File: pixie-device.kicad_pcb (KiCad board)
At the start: 4 copper layers, 70 x 70 mm, 75 parts, among them U1 USBLC6-2SC6, U2 SPX3819M5-L-3-3, U3 W25Q128JVS, U4 ESP32-C3, U5 SN74LVC1T45DBV, Y1 40Mhz

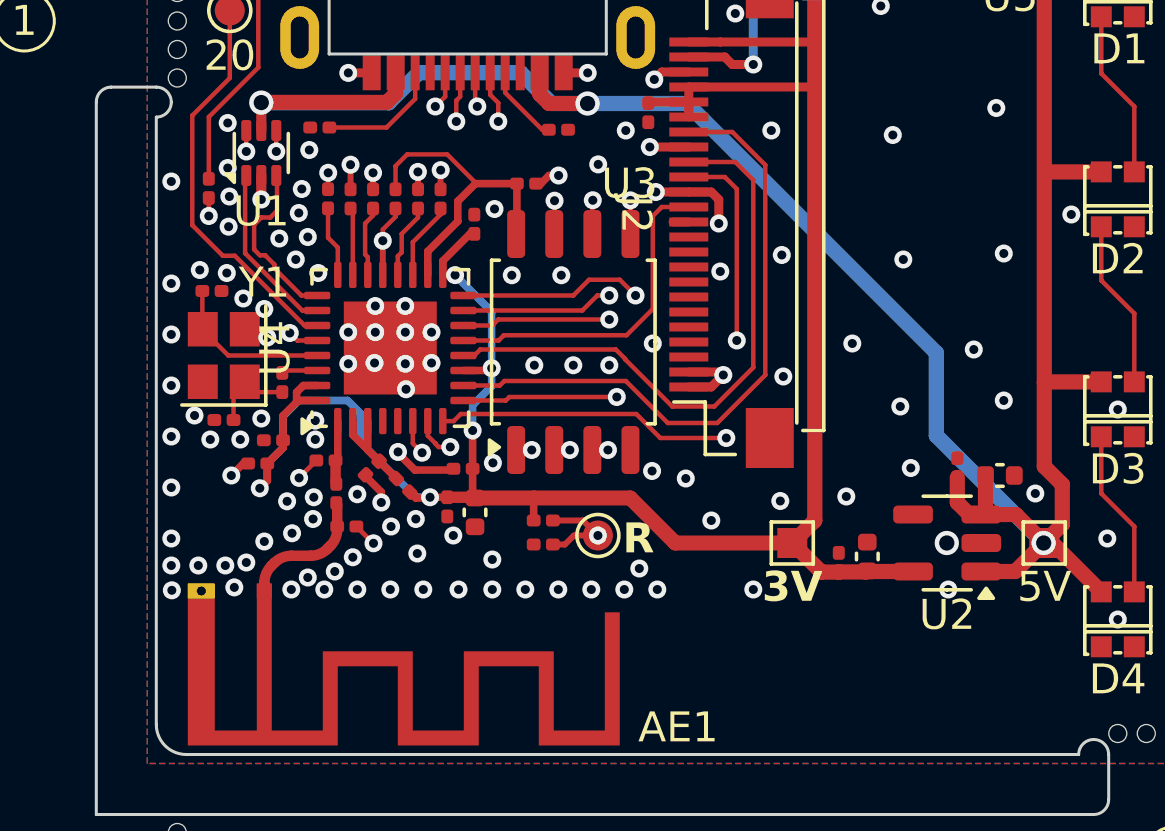
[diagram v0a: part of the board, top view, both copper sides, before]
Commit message: Use ESP suggested C3 footprint and update for KiCad 8.
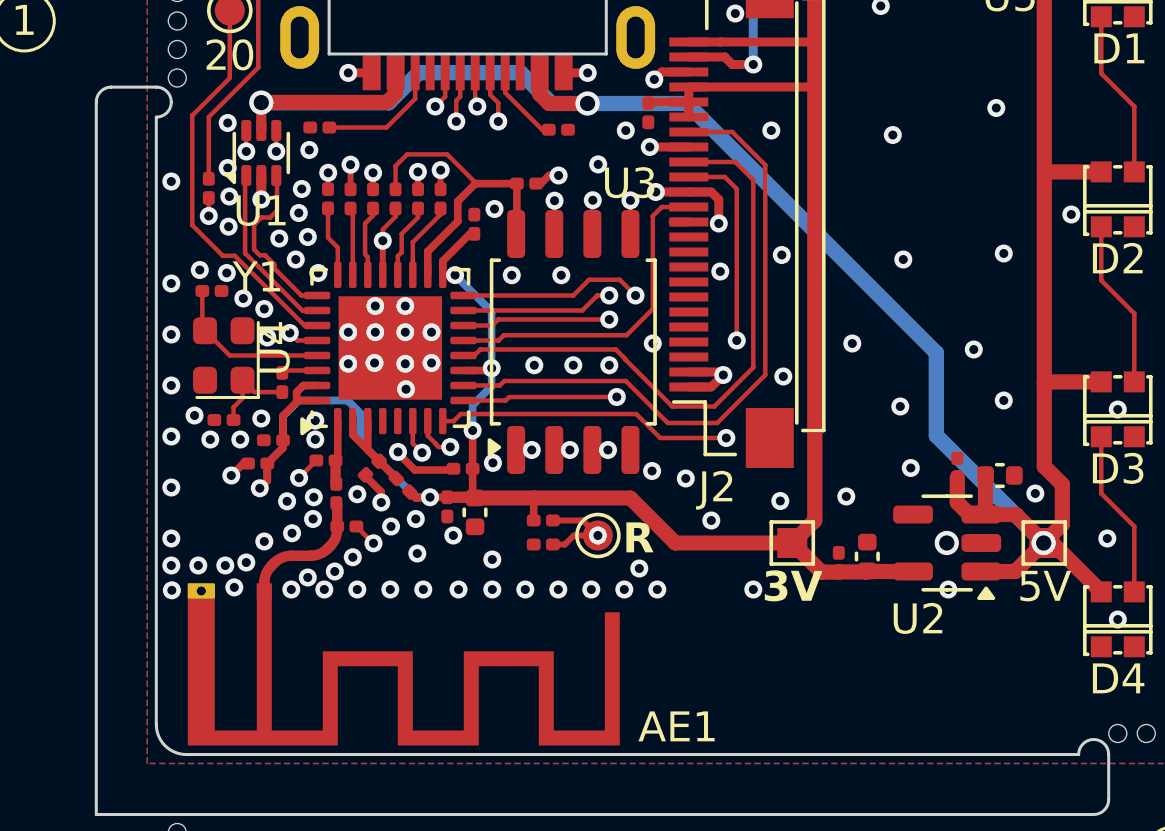
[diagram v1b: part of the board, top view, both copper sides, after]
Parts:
- removed branding-logo-1: logo-15mm, firefly:logo-15mm
- removed branding-name-1: text-10, firefly:text-10
- added REF**: text-10, firefly:text-10, B.Cu at (133.4, 85.0)
- added REF**: logo-15mm, firefly:logo-15mm, B.Cu at (133.1, 78.0)
- U4: footprint Package_DFN_QFN:QFN-32-1EP_5x5mm_P0.5mm_EP3.1x3.1mm -> Package_DFN_QFN:QFN-32-1EP_5x5mm_P0.5mm_EP3.45x3.45mm
- Y1: footprint Crystal:Crystal_SMD_2520-4Pin_2.5x2.0mm -> firefly:crystal_2520

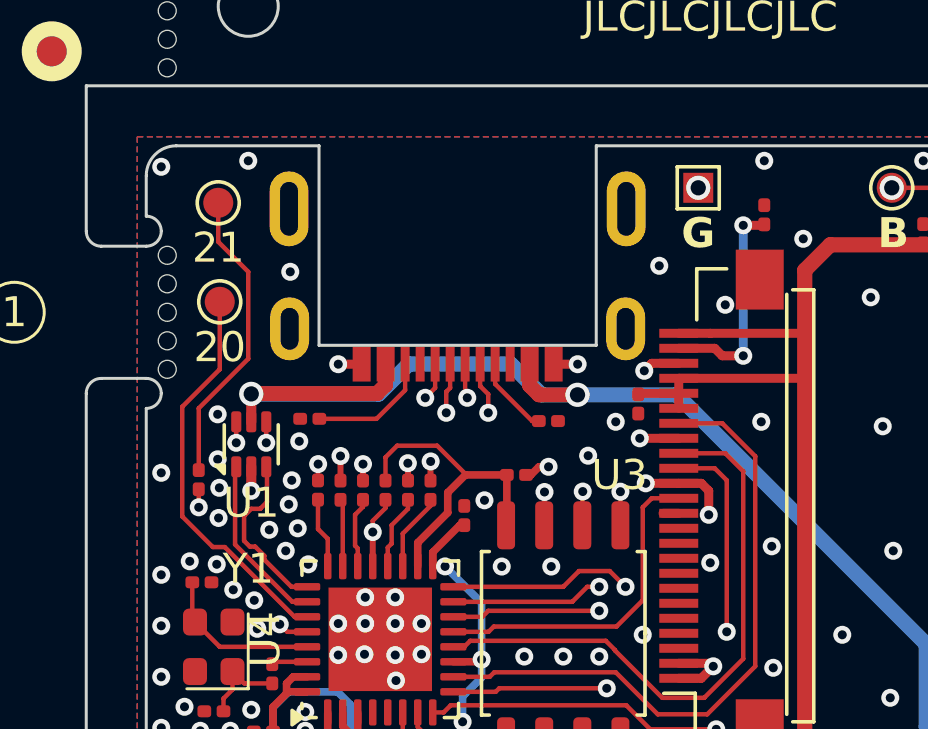
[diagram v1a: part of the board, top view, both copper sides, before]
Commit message: Moved GPIO 20 and 21 around.
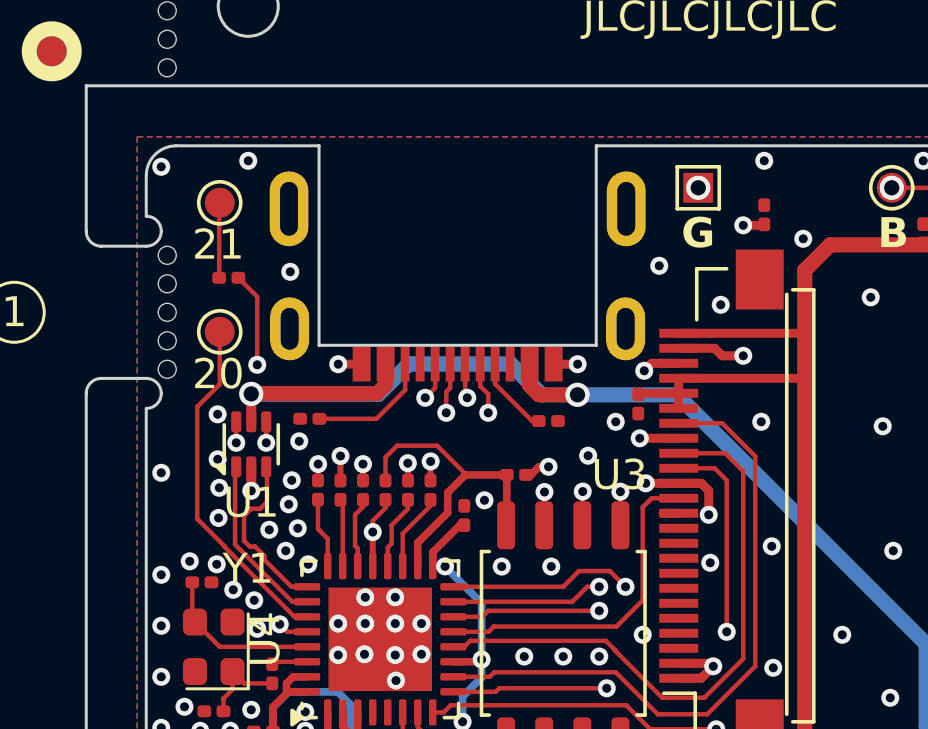
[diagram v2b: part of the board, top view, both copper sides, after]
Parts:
- moved R11 6.80 mm to (102.8, 74.4), turned to 180 degrees
- moved TP1 1.00 mm to (102.5, 76.2)
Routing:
- net Net-(U4-U0TXD/GPIO21): track 6.63 -> 15.1 mm
- net /MCU/IO21: track 10.0 -> 2.51 mm
- net /MCU/IO20: track 13.2 -> 11.6 mm
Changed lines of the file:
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@@
 	(footprint "TestPoint:TestPoint_Pad_D1.0mm"
 		(layer "F.Cu")
-		(at 102.4 71.9)
+		(at 102.45 71.9)
 		(descr "SMD pad as test Point, diameter 1.0mm")
 		(tags "test point SMD pad")
@@
 			(thermal_bridge_angle 45)
 		)
+		(model "${KIPRJMOD}/kicad-components/3d-models/usb-c-sink-8.wrl"
+			(offset
+				(xyz 0 0 0)
+			)
+			(scale
+				(xyz 1 1 1)
+			)
+			(rotate
+				(xyz 0 0 0)
+			)
+		)
 	)
 	(footprint "Capacitor_SMD:C_0201_0603Metric"
@@
 	(footprint "TestPoint:TestPoint_Pad_D1.0mm"
 		(layer "F.Cu")
-		(at 102.45 75.2)
+		(at 102.45 76.2)
 		(descr "SMD pad as test Point, diameter 1.0mm")
 		(tags "test point SMD pad")
@@
 	(footprint "Resistor_SMD:R_0201_0603Metric"
 		(layer "F.Cu")
-		(at 101.75 81.13 90)
+		(at 102.75 74.4 180)
 		(descr "Resistor SMD 0201 (0603 Metric), square (rectangular) end terminal, IPC_7351 nominal, (Body size source: https://www.vishay.com/docs/20052/crcw0201e3.pdf), generated with kicad-footprint-generator")
 		(tags "resistor")
 		(property "Reference" "R11"
-			(at 0 -1.05 90)
+			(at 0 -1.05 180)
 			(layer "F.SilkS")
 			(hide yes)
@@
 		)
 		(property "Value" "499R"
-			(at 0 1.05 90)
+			(at 0 1.05 180)
 			(layer "F.Fab")
 			(effects
@@
 		)
 		(property "Footprint" "Resistor_SMD:R_0201_0603Metric"
-			(at 0 0 90)
+			(at 0 0 180)
 			(unlocked yes)
 			(layer "F.Fab")
@@
 		)
 		(property "Datasheet" ""
-			(at 0 0 90)
+			(at 0 0 180)
 			(unlocked yes)
 			(layer "F.Fab")
@@
 		)
 		(property "Description" ""
-			(at 0 0 90)
+			(at 0 0 180)
 			(unlocked yes)
 			(layer "F.Fab")
@@
 		)
 		(property "MPN" "C4354889"
-			(at 0 0 0)
+			(at 0 0 270)
 			(layer "F.Fab")
 			(hide yes)
@@
 		(attr smd)
 		(fp_line
-			(start 0.7 -0.35)
-			(end 0.7 0.35)
+			(start 0.7 0.35)
+			(end -0.7 0.35)
 			(stroke
 				(width 0.05)
@@
 		)
 		(fp_line
-			(start -0.7 -0.35)
-			(end 0.7 -0.35)
+			(start 0.7 -0.35)
+			(end 0.7 0.35)
 			(stroke
 				(width 0.05)
@@
 		)
 		(fp_line
-			(start 0.7 0.35)
-			(end -0.7 0.35)
+			(start -0.7 0.35)
+			(end -0.7 -0.35)
 			(stroke
 				(width 0.05)
@@
 		)
 		(fp_line
-			(start -0.7 0.35)
-			(end -0.7 -0.35)
+			(start -0.7 -0.35)
+			(end 0.7 -0.35)
 			(stroke
 				(width 0.05)
@@
 		)
 		(fp_line
-			(start 0.3 -0.15)
-			(end 0.3 0.15)
+			(start 0.3 0.15)
+			(end -0.3 0.15)
 			(stroke
 				(width 0.1)
@@
 		)
 		(fp_line
-			(start -0.3 -0.15)
-			(end 0.3 -0.15)
+			(start 0.3 -0.15)
+			(end 0.3 0.15)
 			(stroke
 				(width 0.1)
@@
 		)
 		(fp_line
-			(start 0.3 0.15)
-			(end -0.3 0.15)
+			(start -0.3 0.15)
+			(end -0.3 -0.15)
 			(stroke
 				(width 0.1)
@@
 		)
 		(fp_line
-			(start -0.3 0.15)
-			(end -0.3 -0.15)
+			(start -0.3 -0.15)
+			(end 0.3 -0.15)
 			(stroke
 				(width 0.1)
@@
 		)
 		(fp_text user "${REFERENCE}"
-			(at 0 -0.68 90)
+			(at 0 -0.68 180)
 			(layer "F.Fab")
 			(effects
@@
 		)
 		(pad "" smd roundrect
-			(at -0.345 0 90)
+			(at -0.345 0 180)
 			(size 0.318 0.36)
 			(layers "F.Paste")
@@
 		)
 		(pad "" smd roundrect
-			(at 0.345 0 90)
+			(at 0.345 0 180)
 			(size 0.318 0.36)
 			(layers "F.Paste")
@@
 		)
 		(pad "1" smd roundrect
-			(at -0.32 0 90)
+			(at -0.32 0 180)
 			(size 0.46 0.4)
 			(layers "F.Cu" "F.Mask")
@@
 		)
 		(pad "2" smd roundrect
-			(at 0.32 0 90)
+			(at 0.32 0 180)
 			(size 0.46 0.4)
 			(layers "F.Cu" "F.Mask")
@@
 	)
 	(gr_text "20"
-		(at 102.45 77.3 0)
+		(at 102.4 78.2 0)
 		(layer "F.SilkS")
 		(effects
@@
 	)
 	(gr_text "21"
-		(at 102.4 73.4 0)
+		(at 102.4 73.3 0)
 		(layer "F.SilkS")
 		(effects
@@
 	)
 	(via
-		(at 119.3 75.3)
+		(at 119.15 75.3)
 		(size 0.6)
 		(drill 0.3)
@@
 	)
 	(segment
-		(start 103.4 74.2)
-		(end 102.4 73.2)
-		(width 0.15)
-		(layer "F.Cu")
-		(net 38)
-	)
-	(segment
-		(start 102.4 73.2)
-		(end 102.4 71.9)
+		(start 102.45 71.9)
+		(end 102.43 71.92)
 		(width 0.15)
 		(layer "F.Cu")
@@
 	)
 	(segment
-		(start 103.4 77.1)
-		(end 103.4 74.2)
-		(width 0.15)
-		(layer "F.Cu")
-		(net 38)
-	)
-	(segment
-		(start 101.75 78.75)
-		(end 103.4 77.1)
-		(width 0.15)
-		(layer "F.Cu")
-		(net 38)
-	)
-	(segment
-		(start 101.75 80.81)
-		(end 101.75 78.75)
+		(start 102.43 71.92)
+		(end 102.43 74.4)
 		(width 0.15)
 		(layer "F.Cu")
@@
 		(end 119.9 72.65)
 		(width 0.3)
-		(layer "B.Cu")
+		(layer "In2.Cu")
 		(net 50)
 	)
@@
 	)
 	(segment
-		(start 101.75 82.05)
-		(end 101.75 81.45)
+		(start 103.7 77.3)
+		(end 103.7 75.03)
+		(width 0.15)
+		(layer "F.Cu")
+		(net 51)
+	)
+	(segment
+		(start 103.7 75.03)
+		(end 103.07 74.4)
 		(width 0.15)
 		(layer "F.Cu")
@@
 	)
 	(via
-		(at 101.75 82.05)
+		(at 103.7 77.3)
 		(size 0.6)
 		(drill 0.3)
@@
 	)
 	(segment
-		(start 101.75 82.5)
-		(end 104.45 85.2)
+		(start 104.45 85.2)
+		(end 104.45 85.95)
 		(width 0.15)
 		(layer "In2.Cu")
@@
 	)
 	(segment
-		(start 104.45 85.2)
-		(end 104.45 85.95)
+		(start 103.7 77.3)
+		(end 103.1 77.3)
 		(width 0.15)
 		(layer "In2.Cu")
@@
 	)
 	(segment
-		(start 101.75 82.05)
-		(end 101.75 82.5)
+		(start 103.1 77.3)
+		(end 101.7 78.7)
 		(width 0.15)
 		(layer "In2.Cu")
@@
 	)
 	(segment
-		(start 104.942463 85.7)
-		(end 105.3625 85.7)
+		(start 101.7 82.45)
+		(end 104.45 85.2)
+		(width 0.15)
+		(layer "In2.Cu")
+		(net 51)
+	)
+	(segment
+		(start 101.7 78.7)
+		(end 101.7 82.45)
+		(width 0.15)
+		(layer "In2.Cu")
+		(net 51)
+	)
+	(segment
+		(start 102.45 76.2)
+		(end 102.45 77.95)
 		(width 0.15)
 		(layer "F.Cu")
@@
 	)
 	(segment
-		(start 102.617463 83.375)
-		(end 104.942463 85.7)
+		(start 104.942463 85.7)
+		(end 105.3625 85.7)
 		(width 0.15)
 		(layer "F.Cu")
@@
 	)
 	(segment
-		(start 102.45 77.45)
-		(end 101.2 78.7)
+		(start 102.617463 83.355147)
+		(end 102.617463 83.375)
 		(width 0.15)
 		(layer "F.Cu")
@@
 	)
 	(segment
-		(start 102.45 75.2)
-		(end 102.45 77.45)
+		(start 101.7 78.7)
+		(end 101.7 82.437684)
 		(width 0.15)
 		(layer "F.Cu")
@@
 	)
 	(segment
-		(start 102.218037 83.375)
-		(end 102.617463 83.375)
+		(start 101.7 82.437684)
+		(end 102.617463 83.355147)
 		(width 0.15)
 		(layer "F.Cu")
@@
 	)
 	(segment
-		(start 101.2 82.356963)
-		(end 102.218037 83.375)
+		(start 102.617463 83.375)
+		(end 104.942463 85.7)
 		(width 0.15)
 		(layer "F.Cu")
@@
 	)
 	(segment
-		(start 101.2 78.7)
-		(end 101.2 82.356963)
+		(start 102.45 77.95)
+		(end 101.7 78.7)
 		(width 0.15)
 		(layer "F.Cu")

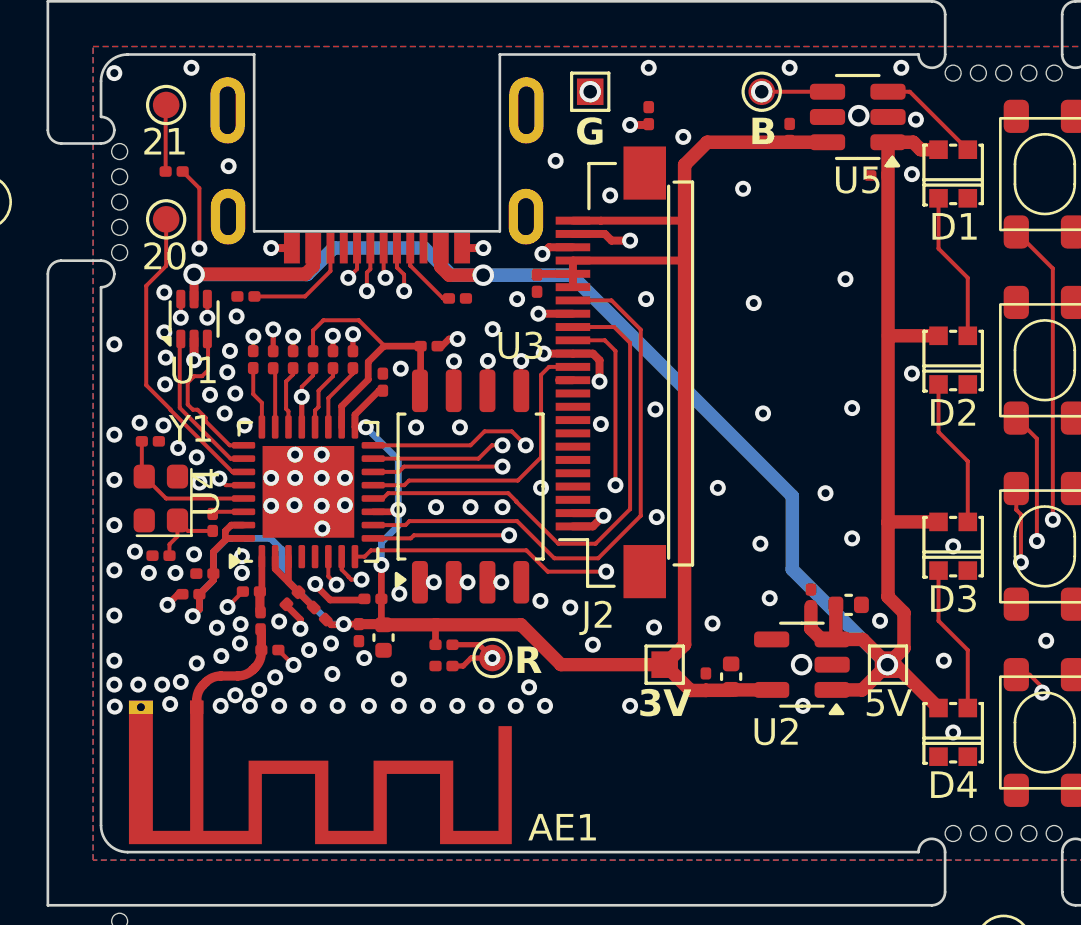
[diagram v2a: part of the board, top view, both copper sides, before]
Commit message: Tweaked placements; GPIO 20 and 21.
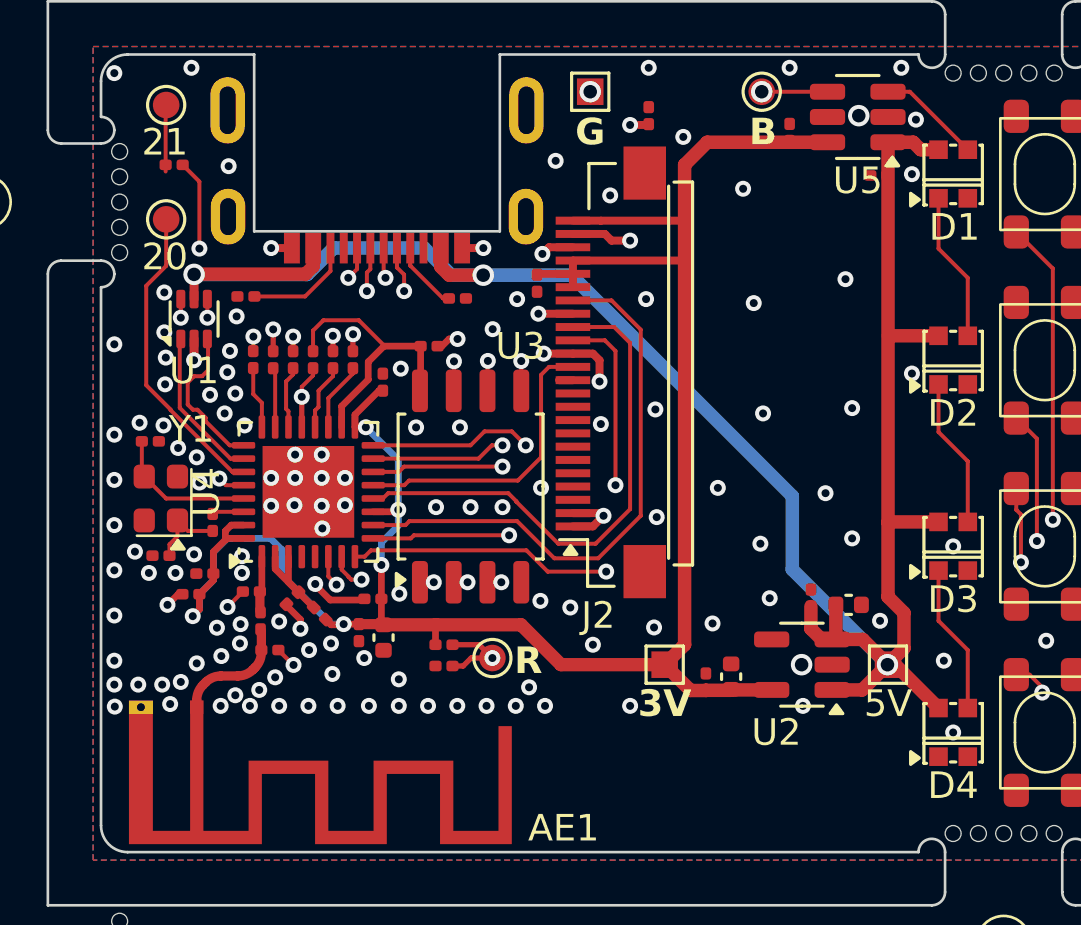
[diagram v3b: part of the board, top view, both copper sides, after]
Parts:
- moved R11 0.25 mm to (102.8, 74.2)
